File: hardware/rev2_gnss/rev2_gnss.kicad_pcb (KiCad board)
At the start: 2 copper layers, 33 x 24 mm, 22 parts, among them J1 Conn_01x06, U1 SAM-M10Q

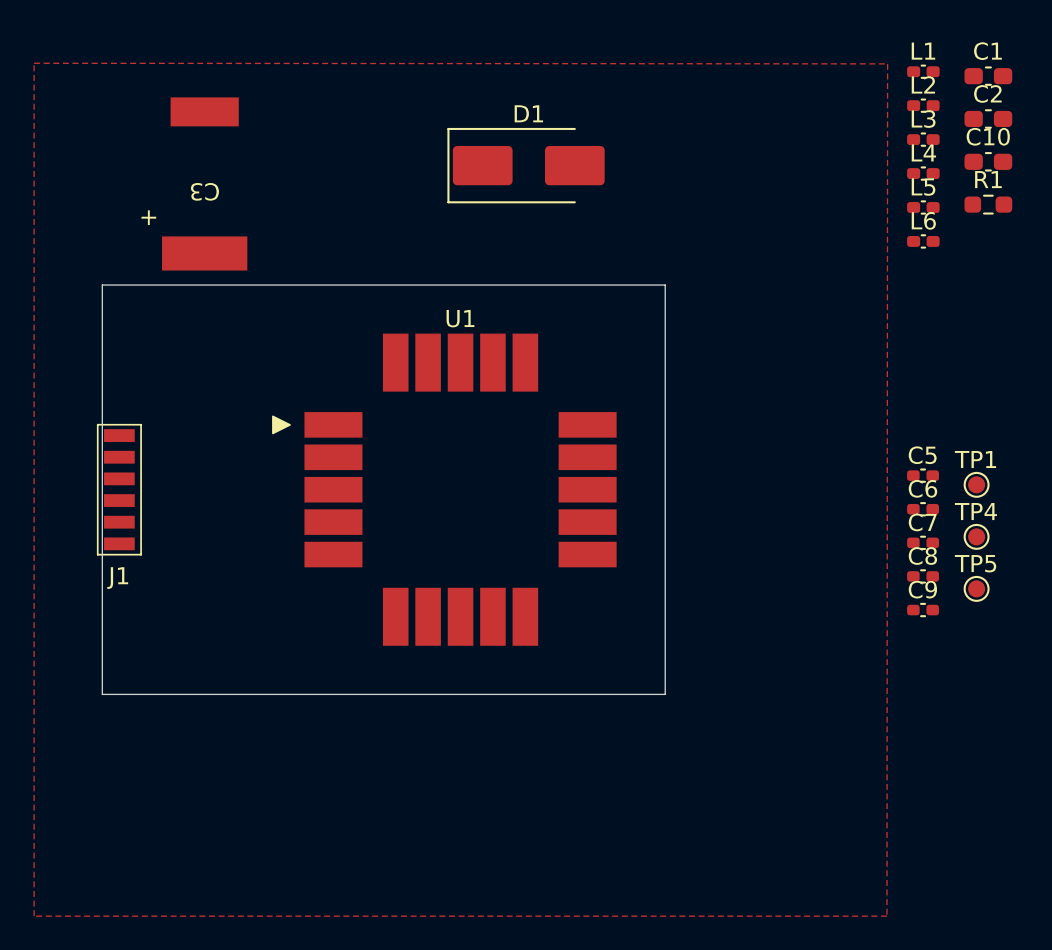
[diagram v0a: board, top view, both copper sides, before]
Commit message: gnss layout
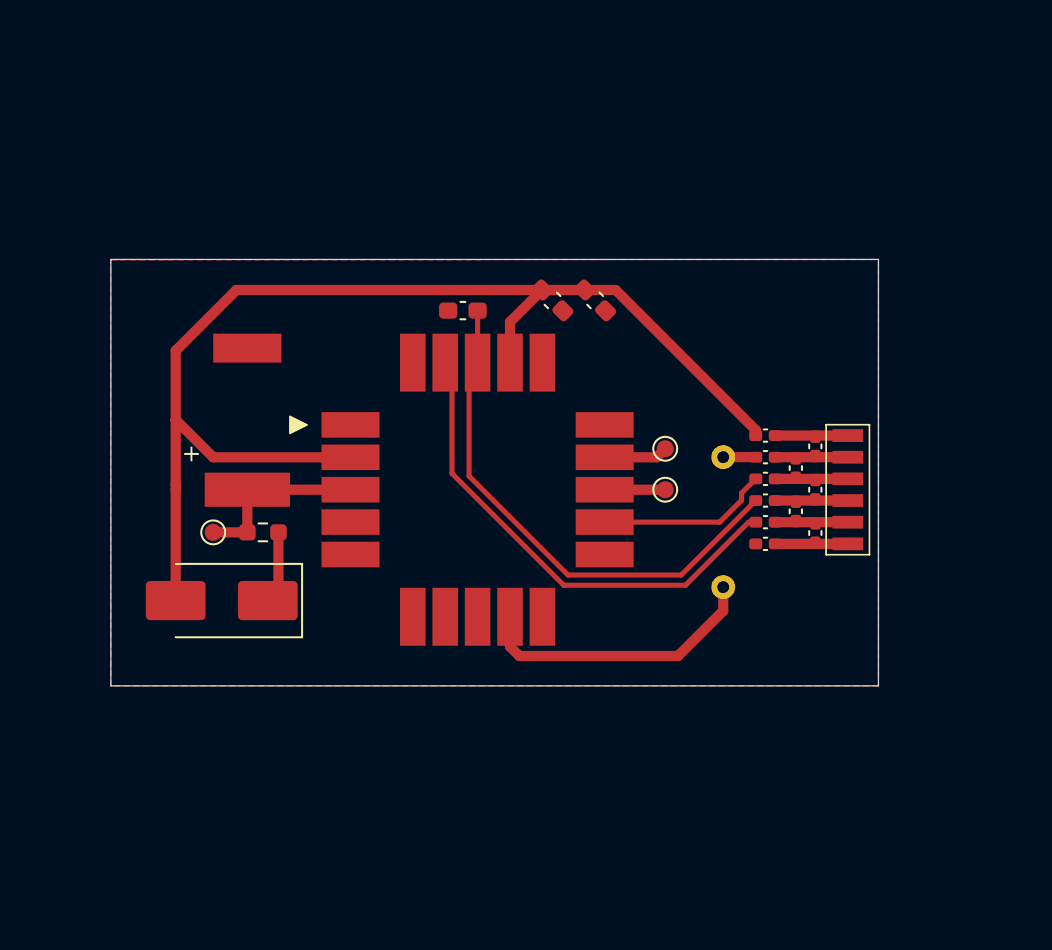
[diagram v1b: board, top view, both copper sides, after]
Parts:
- added R2: 0 R, Resistor_THT:R_Axial_DIN0204_L3.6mm_D1.6mm_P7.62mm_Horizontal, B.Cu at (164.4, 98.1)
- moved R1 46.7 mm to (137.4, 102.5), turned to 180 degrees
- moved TP1 44.8 mm to (134.5, 102.5)
- moved J1 42.7 mm to (171.7, 100.0)
- moved C10 32.0 mm to (149.1, 89.5), turned to 180 degrees
- moved D1 31.2 mm to (135.0, 106.5), turned to 180 degrees
- moved C2 27.7 mm to (154.4, 88.9), turned to 135 degrees
- moved C1 26.5 mm to (156.9, 88.9), turned to -45 degrees
- moved L1 23.3 mm to (166.9, 96.8), turned to 180 degrees
- moved L2 22.6 mm to (166.9, 98.1), turned to 180 degrees
- moved L3 21.9 mm to (166.9, 99.4), turned to 180 degrees
- moved L4 21.3 mm to (166.9, 100.6), turned to 180 degrees
- moved L5 20.6 mm to (166.9, 101.9), turned to 180 degrees
- moved TP5 20.0 mm to (161.0, 97.6)
- moved L6 20.0 mm to (166.9, 103.2), turned to 180 degrees
- moved TP4 18.5 mm to (161.0, 100.0)
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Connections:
- C5 pad 2: Net-(C5-Pad2) -> Net-(J1-Pin_2)
- C6 pad 1: Net-(C5-Pad2) -> Net-(J1-Pin_2)
- C6 pad 2: Net-(C6-Pad2) -> Net-(J1-Pin_3)
- C7 pad 1: Net-(C6-Pad2) -> Net-(J1-Pin_3)
- C7 pad 2: Net-(C7-Pad2) -> Net-(J1-Pin_4)
- C8 pad 1: Net-(C7-Pad2) -> Net-(J1-Pin_4)
- L2 pad 2: /SDA -> Net-(L2-Pad2)
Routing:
- net +3V3: track 0.00 -> 70.1 mm
- net /RESET_N: track 0.00 -> 30.9 mm
- net /EXTINT: track 0.00 -> 28.7 mm
- net /SDA: track 0.00 -> 17.0 mm
- net /+BACKUP: track 0.00 -> 10.6 mm
- net /SCL: track 0.00 -> 10.2 mm
- net Net-(D1-K): track 0.00 -> 4.26 mm
- net Net-(J1-Pin_6): track 0.00 -> 4.25 mm
- net Net-(J1-Pin_5): track 0.00 -> 4.25 mm
- net Net-(J1-Pin_4): track 0.00 -> 4.25 mm
- net Net-(J1-Pin_3): track 0.00 -> 4.25 mm
- net Net-(J1-Pin_2): track 0.00 -> 4.25 mm
- net Net-(J1-Pin_1): track 0.00 -> 4.25 mm
- net Net-(U1-RXD): track 0.00 -> 3.76 mm
- net Net-(U1-TXD): track 0.00 -> 3.55 mm
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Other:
- board size 33 x 24 mm -> 45 x 25 mm

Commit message: changed values to what was ordered
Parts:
- C5, C6, C7, C8, C9: value 3 nF -> 3000 pF
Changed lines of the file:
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@@
 			)
 		)
-		(property "Value" "3 nF"
+		(property "Value" "3000 pF"
 			(at 0 1.16 90)
 			(layer "F.Fab")
@@
 			)
 		)
-		(property "Value" "3 nF"
+		(property "Value" "3000 pF"
 			(at 0 1.16 90)
 			(layer "F.Fab")
@@
 			)
 		)
-		(property "Value" "3 nF"
+		(property "Value" "3000 pF"
 			(at 0 1.16 90)
 			(layer "F.Fab")
@@
 		(sheetname "/")
 		(sheetfile "rev2_gnss.kicad_sch")
+		(units
+			(unit
+				(name "A")
+				(pins "1" "2")
+			)
+		)
 		(attr smd)
 		(duplicate_pad_numbers_are_jumpers no)
@@
 			)
 		)
-		(property "Value" "3 nF"
+		(property "Value" "3000 pF"
 			(at 0 1.16 90)
 			(layer "F.Fab")
@@
 			)
 		)
-		(property "Value" "3 nF"
+		(property "Value" "3000 pF"
 			(at 0 1.16 90)
 			(layer "F.Fab")
@@
 		(sheetname "/")
 		(sheetfile "rev2_gnss.kicad_sch")
+		(units
+			(unit
+				(name "A")
+				(pins "1" "2")
+			)
+		)
 		(attr through_hole)
 		(duplicate_pad_numbers_are_jumpers no)
